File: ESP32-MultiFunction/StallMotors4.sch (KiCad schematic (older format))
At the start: 0 parts

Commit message: Working on ESP32-MultiFunction.
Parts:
- added C6, C7: .1 uf, Capacitors_SMD:C_0603, symbol C_Small
- added RR1: 10K Ohms, 48xxP:4814P, symbol 4814P-2
- added Term1: Motor 1, Connectors_Terminal_Blocks:TerminalBlock_Pheonix_MPT-2.54mm_5pol, symbol Screw_Terminal_01x05
- added Term2: Motor 2, Connectors_Terminal_Blocks:TerminalBlock_Pheonix_MPT-2.54mm_5pol, symbol Screw_Terminal_01x05
- added Term3: Motor 3, Connectors_Terminal_Blocks:TerminalBlock_Pheonix_MPT-2.54mm_5pol, symbol Screw_Terminal_01x05
- added Term4: Motor 4, Connectors_Terminal_Blocks:TerminalBlock_Pheonix_MPT-2.54mm_5pol, symbol Screw_Terminal_01x05
- added Term5: + 12V -, symbol Screw_Terminal_01x02
- added U2, U4: 74HCT00, Housings_SOIC:SOIC-14_3.9x8.7mm_Pitch1.27mm, symbol 74HCT00
- added U5, U6, U7, U8: TC4428, Housings_SOIC:SOIC-8_3.9x4.9mm_Pitch1.27mm, symbol TC4428
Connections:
- new net: U2.2, U2.6
- new net: U2.10, U2.11
- new net: U4.2, U4.6
- new net: U4.10, U4.11
- new net +12V: Term5.1 (Pin_1), U5.6 (Vdd), U5.6 (Vdd), U6.6 (Vdd), U6.6 (Vdd), U7.6 (Vdd), U7.6 (Vdd), U8.6 (Vdd), U8.6 (Vdd)
- new net +3V3: C6.1, C7.1, RR1.14 (Comm), U2.14 (VCC), U2.14 (VCC), U2.14 (VCC), U2.14 (VCC), U4.14 (VCC), U4.14 (VCC), U4.14 (VCC), U4.14 (VCC)
- new net GND: C6.2, C7.2, Term1.4 (Pin_4), Term2.4 (Pin_4), Term3.4 (Pin_4), Term4.4 (Pin_4), Term5.2 (Pin_2), U2.7 (GND), U2.7 (GND), U2.7 (GND), U2.7 (GND), U4.7 (GND), U4.7 (GND), U4.7 (GND), U4.7 (GND), U5.3 (GND), U5.3 (GND), U6.3 (GND), U6.3 (GND), U7.3 (GND), U7.3 (GND), U8.3 (GND), U8.3 (GND)
- new net M1A: Term1.1 (Pin_1), U5.7 (Out)
- new net M1B: Term1.2 (Pin_2), U5.5 (Out)
- new net M2A: Term2.1 (Pin_1), U6.7 (Out)
- new net M2B: Term2.2 (Pin_2), U6.5 (Out)
- new net M3A: Term3.1 (Pin_1), U7.7 (Out)
- new net M3B: Term3.2 (Pin_2), U7.5 (Out)
- new net M4A: Term4.1 (Pin_1), U8.7 (Out)
- new net M4B: Term4.2 (Pin_2), U8.5 (Out)
- new net Motor1: U5.2 (IN), U5.4 (IN)
- new net Motor2: U6.2 (IN), U6.4 (IN)
- new net Motor3: U7.2 (IN), U7.4 (IN)
- new net Motor4: U8.2 (IN), U8.4 (IN)
- new net P1A: RR1.6 (R6), Term1.3 (Pin_3), U2.1
- new net P1B: RR1.5 (R5), Term1.5 (Pin_5), U2.5
- new net P2A: RR1.4 (R4), Term2.3 (Pin_3), U2.9
- new net P2B: RR1.3 (R3), Term2.5 (Pin_5), U2.13
- new net P3A: RR1.13 (R13), Term3.3 (Pin_3), U4.1
- new net P3B: RR1.12 (R12), Term3.5 (Pin_5), U4.5
- new net P4A: RR1.11 (R11), Term4.3 (Pin_3), U4.9
- new net P4B: RR1.10 (R10), Term4.5 (Pin_5), U4.13
- new net Points1: U2.3, U2.4
- new net Points2: U2.12, U2.8
- new net Points3: U4.3, U4.4
- new net Points4: U4.12, U4.8
- no-connect marks 0 -> 5

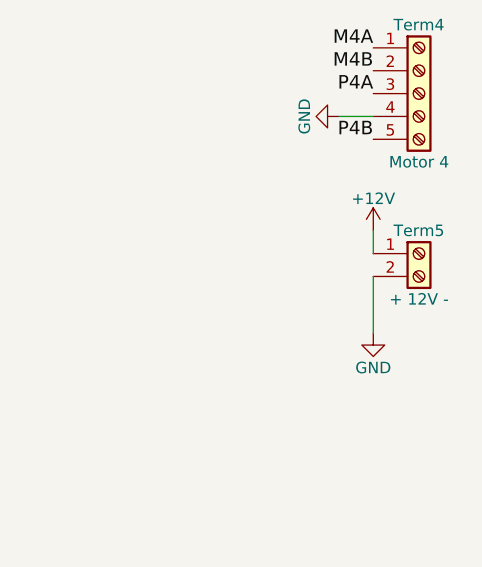
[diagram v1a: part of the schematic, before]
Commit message: Working on ESP32-MultiFunction.
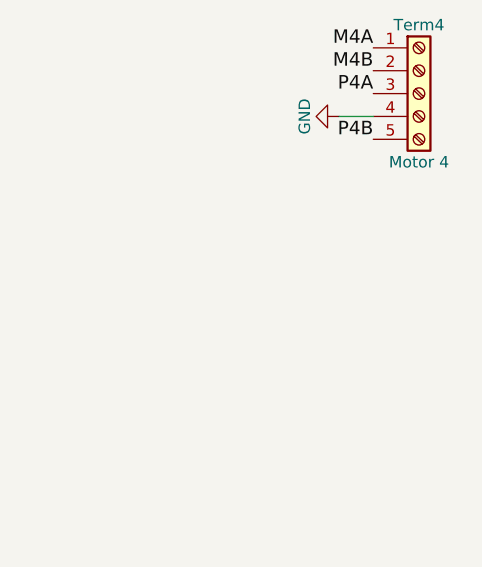
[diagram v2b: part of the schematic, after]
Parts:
- removed Term5: + 12V -, symbol Screw_Terminal_01x02
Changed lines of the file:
@@
 $Descr A4 11693 8268
 encoding utf-8
-Sheet 6 8
+Sheet 6 7
 Title "ESP32 Multifunction board"
 Date ""
@@
 	4500 2100 4500 2150
 $Comp
-L Screw_Terminal_01x02 Term5
-U 1 1 60CDEFA9
-P 10000 4300
-F 0 "Term5" H 10000 4400 50  0000 C CNN
-F 1 "+ 12V -" H 10000 4100 50  0000 C CNN
-F 2 "" H 10000 4300 50  0001 C CNN
-F 3 "" H 10000 4300 50  0001 C CNN
-	1    10000 4300
-	1    0    0    -1
-$EndComp
-$Comp
-L +12V #PWR45
-U 1 1 60CDEFFA
-P 9800 4200
-F 0 "#PWR45" H 9800 4050 50  0001 C CNN
-F 1 "+12V" H 9800 4340 50  0000 C CNN
-F 2 "" H 9800 4200 50  0001 C CNN
-F 3 "" H 9800 4200 50  0001 C CNN
-	1    9800 4200
-	1    0    0    -1
-$EndComp
-$Comp
-L GND #PWR46
-U 1 1 60CDF03E
-P 9800 4650
-F 0 "#PWR46" H 9800 4400 50  0001 C CNN
-F 1 "GND" H 9800 4500 50  0000 C CNN
-F 2 "" H 9800 4650 50  0001 C CNN
-F 3 "" H 9800 4650 50  0001 C CNN
-	1    9800 4650
-	1    0    0    -1
-$EndComp
-$Comp
 L GND #PWR42
 U 1 1 60CDF082
@@
 Wire Wire Line
 	9800 3700 9650 3700
-Wire Wire Line
-	9800 4200 9800 4300
-Wire Wire Line
-	9800 4400 9800 4650
 Text Label 9800 800  2    59   ~ 0
 M1A

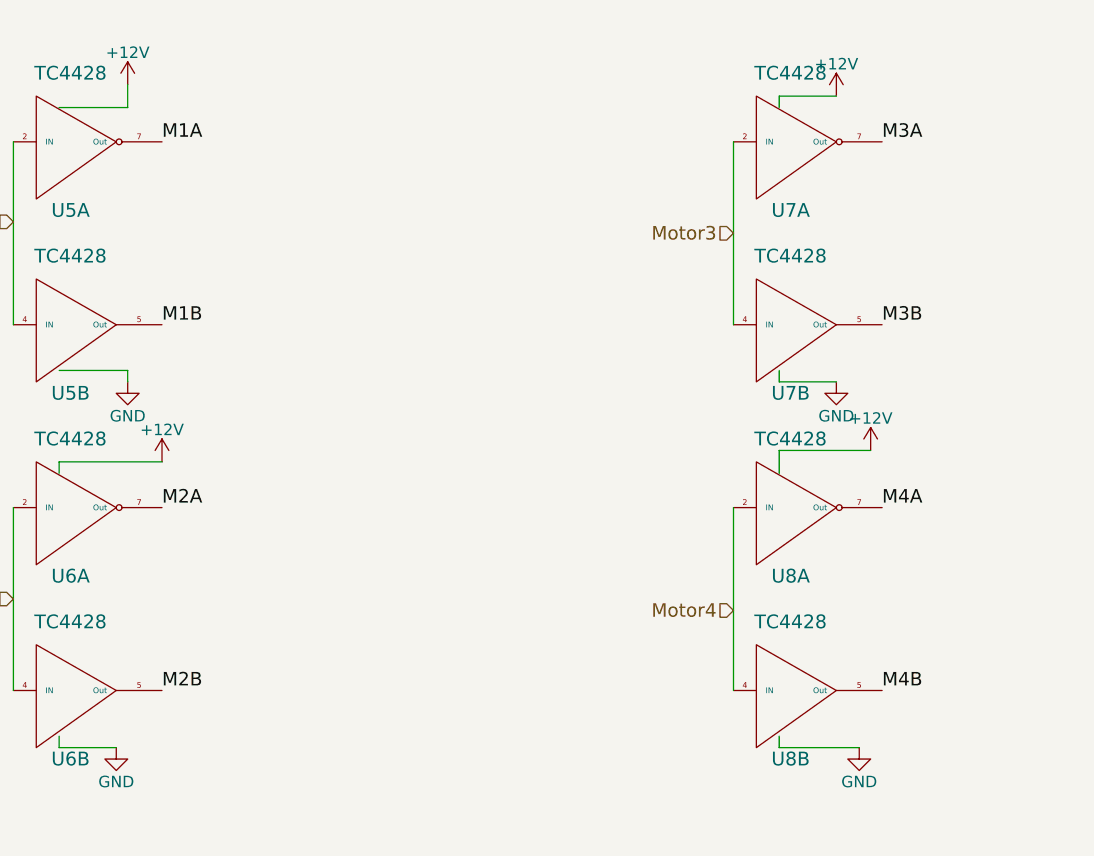
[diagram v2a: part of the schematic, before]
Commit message: Working on ESP32-MultiFunction.
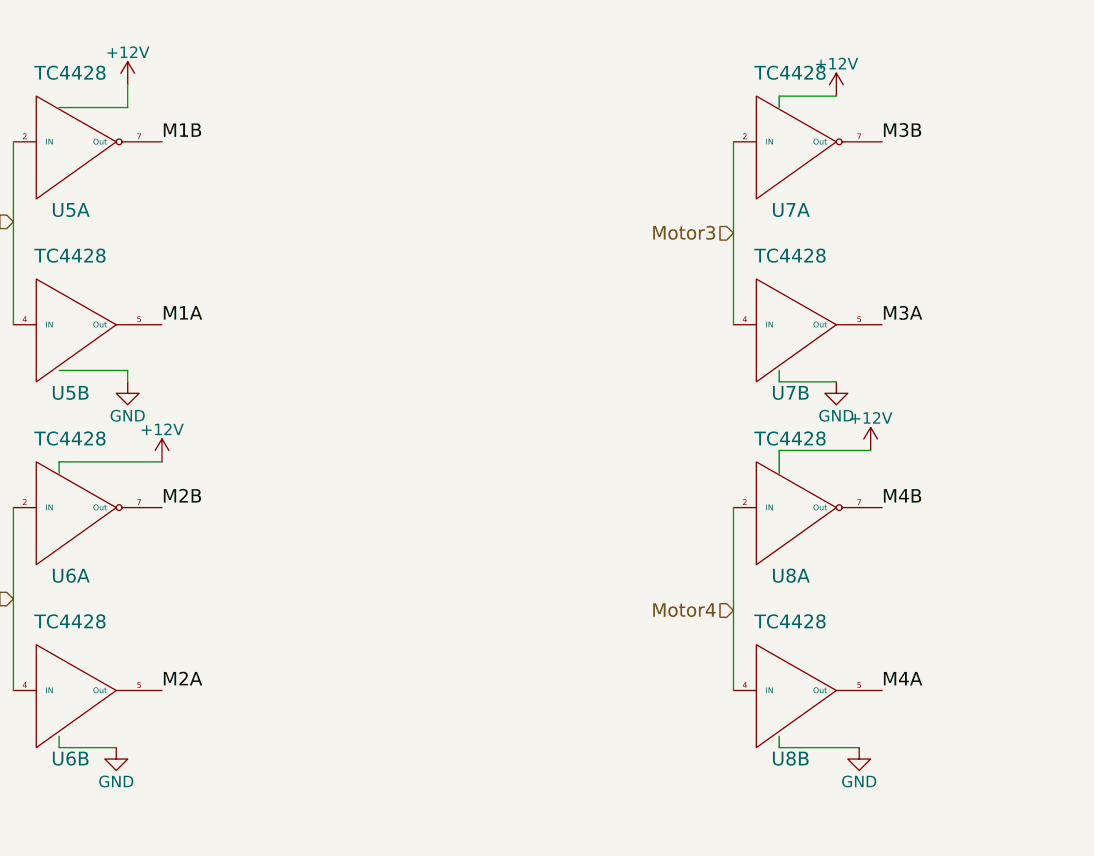
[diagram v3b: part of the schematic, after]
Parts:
- U2, U4: footprint (none) -> Housings_SOIC:SOIC-14_3.9x8.7mm_Pitch1.27mm
- U5, U6, U7, U8: footprint (none) -> Housings_SOIC:SOIC-8_3.9x4.9mm_Pitch1.27mm
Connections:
- net M1A: now also U5.5 (Out); no longer U5.7 (Out)
- net M1B: now also U5.7 (Out); no longer U5.5 (Out)
- net M2A: now also U6.5 (Out); no longer U6.7 (Out)
- net M2B: now also U6.7 (Out); no longer U6.5 (Out)
- net M3A: now also U7.5 (Out); no longer U7.7 (Out)
- net M3B: now also U7.7 (Out); no longer U7.5 (Out)
- net M4A: now also U8.5 (Out); no longer U8.7 (Out)
- net M4B: now also U8.7 (Out); no longer U8.5 (Out)
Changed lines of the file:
@@
 F 0 "U2" H 2000 1950 50  0000 C CNN
 F 1 "74HCT00" H 2000 1800 50  0000 C CNN
-F 2 "" H 2000 1900 50  0001 C CNN
+F 2 "Housings_SOIC:SOIC-14_3.9x8.7mm_Pitch1.27mm" H 2000 1900 50  0001 C CNN
 F 3 "" H 2000 1900 50  0001 C CNN
 	2    2000 1900
@@
 F 0 "U2" H 2000 2750 50  0000 C CNN
 F 1 "74HCT00" H 2000 2600 50  0000 C CNN
-F 2 "" H 2000 2700 50  0001 C CNN
+F 2 "Housings_SOIC:SOIC-14_3.9x8.7mm_Pitch1.27mm" H 2000 2700 50  0001 C CNN
 F 3 "" H 2000 2700 50  0001 C CNN
 	3    2000 2700
@@
 F 0 "U2" H 2000 3450 50  0000 C CNN
 F 1 "74HCT00" H 2000 3300 50  0000 C CNN
-F 2 "" H 2000 3400 50  0001 C CNN
+F 2 "Housings_SOIC:SOIC-14_3.9x8.7mm_Pitch1.27mm" H 2000 3400 50  0001 C CNN
 F 3 "" H 2000 3400 50  0001 C CNN
 	4    2000 3400
@@
 F 0 "U4" H 2050 5350 50  0000 C CNN
 F 1 "74HCT00" H 2050 5200 50  0000 C CNN
-F 2 "" H 2050 5300 50  0001 C CNN
+F 2 "Housings_SOIC:SOIC-14_3.9x8.7mm_Pitch1.27mm" H 2050 5300 50  0001 C CNN
 F 3 "" H 2050 5300 50  0001 C CNN
 	2    2050 5300
@@
 F 0 "U4" H 2050 6150 50  0000 C CNN
 F 1 "74HCT00" H 2050 6000 50  0000 C CNN
-F 2 "" H 2050 6100 50  0001 C CNN
+F 2 "Housings_SOIC:SOIC-14_3.9x8.7mm_Pitch1.27mm" H 2050 6100 50  0001 C CNN
 F 3 "" H 2050 6100 50  0001 C CNN
 	3    2050 6100
@@
 F 0 "U4" H 2050 6850 50  0000 C CNN
 F 1 "74HCT00" H 2050 6700 50  0000 C CNN
-F 2 "" H 2050 6800 50  0001 C CNN
+F 2 "Housings_SOIC:SOIC-14_3.9x8.7mm_Pitch1.27mm" H 2050 6800 50  0001 C CNN
 F 3 "" H 2050 6800 50  0001 C CNN
 	4    2050 6800
@@
 F 0 "U5" H 4250 1600 60  0000 C CNN
 F 1 "TC4428" H 4250 2200 60  0000 C CNN
-F 2 "" H 4250 1900 60  0000 C CNN
+F 2 "Housings_SOIC:SOIC-8_3.9x4.9mm_Pitch1.27mm" H 4250 1900 60  0001 C CNN
 F 3 "" H 4250 1900 60  0000 C CNN
 	2    4250 1900
@@
 F 0 "U6" H 4250 3200 60  0000 C CNN
 F 1 "TC4428" H 4250 3800 60  0000 C CNN
-F 2 "" H 4250 3500 60  0000 C CNN
+F 2 "Housings_SOIC:SOIC-8_3.9x4.9mm_Pitch1.27mm" H 4250 3500 60  0001 C CNN
 F 3 "" H 4250 3500 60  0000 C CNN
 	2    4250 3500
@@
 F 0 "U7" H 7400 1600 60  0000 C CNN
 F 1 "TC4428" H 7400 2200 60  0000 C CNN
-F 2 "" H 7400 1900 60  0000 C CNN
+F 2 "Housings_SOIC:SOIC-8_3.9x4.9mm_Pitch1.27mm" H 7400 1900 60  0001 C CNN
 F 3 "" H 7400 1900 60  0000 C CNN
 	2    7400 1900
@@
 F 0 "U8" H 7400 3200 60  0000 C CNN
 F 1 "TC4428" H 7400 3800 60  0000 C CNN
-F 2 "" H 7400 3500 60  0000 C CNN
+F 2 "Housings_SOIC:SOIC-8_3.9x4.9mm_Pitch1.27mm" H 7400 3500 60  0001 C CNN
 F 3 "" H 7400 3500 60  0000 C CNN
 	2    7400 3500
@@
 $Comp
 L Screw_Terminal_01x05 Term1
-U 1 1 60CD6A0E
+U 1 1 60CF9376
 P 10000 1000
 F 0 "Term1" H 10000 1300 50  0000 C CNN
@@
 $EndComp
 $Comp
-L +3V3 #PWR28
+L +3V3 #PWR036
 U 1 1 60CD8400
 P 1800 750
-F 0 "#PWR28" H 1800 600 50  0001 C CNN
+F 0 "#PWR036" H 1800 600 50  0001 C CNN
 F 1 "+3V3" H 1800 890 50  0000 C CNN
 F 2 "" H 1800 750 50  0001 C CNN
@@
 $EndComp
 $Comp
-L +3V3 #PWR30
+L +3V3 #PWR037
 U 1 1 60CD84B5
 P 1800 4200
-F 0 "#PWR30" H 1800 4050 50  0001 C CNN
+F 0 "#PWR037" H 1800 4050 50  0001 C CNN
 F 1 "+3V3" H 1800 4340 50  0000 C CNN
 F 2 "" H 1800 4200 50  0001 C CNN
@@
 $EndComp
 $Comp
-L GND #PWR29
+L GND #PWR038
 U 1 1 60CD85AF
 P 1800 3800
-F 0 "#PWR29" H 1800 3550 50  0001 C CNN
+F 0 "#PWR038" H 1800 3550 50  0001 C CNN
 F 1 "GND" H 1800 3650 50  0000 C CNN
 F 2 "" H 1800 3800 50  0001 C CNN
@@
 $EndComp
 $Comp
-L GND #PWR31
+L GND #PWR039
 U 1 1 60CD86EE
 P 1850 7200
-F 0 "#PWR31" H 1850 6950 50  0001 C CNN
+F 0 "#PWR039" H 1850 6950 50  0001 C CNN
 F 1 "GND" H 1850 7050 50  0000 C CNN
 F 2 "" H 1850 7200 50  0001 C CNN
@@
 	3200 1050 2850 1050
 $Comp
-L GND #PWR32
+L GND #PWR040
 U 1 1 60CD9FDD
 P 3200 1200
-F 0 "#PWR32" H 3200 950 50  0001 C CNN
+F 0 "#PWR040" H 3200 950 50  0001 C CNN
 F 1 "GND" H 3200 1050 50  0000 C CNN
 F 2 "" H 3200 1200 50  0001 C CNN
@@
 P4B
 Text Label 4650 1100 0    59   ~ 0
+M1B
+Text Label 4650 1900 0    59   ~ 0
 M1A
-Text Label 4650 1900 0    59   ~ 0
-M1B
 Text Label 4650 2700 0    59   ~ 0
+M2B
+Text Label 4650 3500 0    59   ~ 0
 M2A
-Text Label 4650 3500 0    59   ~ 0
-M2B
 Text Label 7800 1100 0    59   ~ 0
+M3B
+Text Label 7800 1900 0    59   ~ 0
 M3A
-Text Label 7800 1900 0    59   ~ 0
-M3B
 Text Label 7800 2700 0    59   ~ 0
+M4B
+Text Label 7800 3500 0    59   ~ 0
 M4A
-Text Label 7800 3500 0    59   ~ 0
-M4B
 Wire Wire Line
 	7150 2700 7150 3500
@@
 Motor4
 $Comp
-L GND #PWR35
+L GND #PWR041
 U 1 1 60CDE058
 P 4500 2150
-F 0 "#PWR35" H 4500 1900 50  0001 C CNN
+F 0 "#PWR041" H 4500 1900 50  0001 C CNN
 F 1 "GND" H 4500 2000 50  0000 C CNN
 F 2 "" H 4500 2150 50  0001 C CNN
@@
 $EndComp
 $Comp
-L GND #PWR38
+L GND #PWR042
 U 1 1 60CDE09A
 P 7600 2150
-F 0 "#PWR38" H 7600 1900 50  0001 C CNN
+F 0 "#PWR042" H 7600 1900 50  0001 C CNN
 F 1 "GND" H 7600 2000 50  0000 C CNN
 F 2 "" H 7600 2150 50  0001 C CNN
@@
 $EndComp
 $Comp
-L GND #PWR33
+L GND #PWR043
 U 1 1 60CDE17D
 P 4450 3750
-F 0 "#PWR33" H 4450 3500 50  0001 C CNN
+F 0 "#PWR043" H 4450 3500 50  0001 C CNN
 F 1 "GND" H 4450 3600 50  0000 C CNN
 F 2 "" H 4450 3750 50  0001 C CNN
@@
 $EndComp
 $Comp
-L GND #PWR39
+L GND #PWR044
 U 1 1 60CDE1BF
 P 7700 3750
-F 0 "#PWR39" H 7700 3500 50  0001 C CNN
+F 0 "#PWR044" H 7700 3500 50  0001 C CNN
 F 1 "GND" H 7700 3600 50  0000 C CNN
 F 2 "" H 7700 3750 50  0001 C CNN
@@
 $EndComp
 $Comp
-L +12V #PWR34
+L +12V #PWR045
 U 1 1 60CDE3F5
 P 4500 850
-F 0 "#PWR34" H 4500 700 50  0001 C CNN
+F 0 "#PWR045" H 4500 700 50  0001 C CNN
 F 1 "+12V" H 4500 990 50  0000 C CNN
 F 2 "" H 4500 850 50  0001 C CNN
@@
 $EndComp
 $Comp
-L +12V #PWR37
+L +12V #PWR046
 U 1 1 60CDE437
 P 7600 900
-F 0 "#PWR37" H 7600 750 50  0001 C CNN
+F 0 "#PWR046" H 7600 750 50  0001 C CNN
 F 1 "+12V" H 7600 1040 50  0000 C CNN
 F 2 "" H 7600 900 50  0001 C CNN
@@
 $EndComp
 $Comp
-L +12V #PWR40
+L +12V #PWR047
 U 1 1 60CDE58D
 P 7750 2450
-F 0 "#PWR40" H 7750 2300 50  0001 C CNN
+F 0 "#PWR047" H 7750 2300 50  0001 C CNN
 F 1 "+12V" H 7750 2590 50  0000 C CNN
 F 2 "" H 7750 2450 50  0001 C CNN
@@
 $EndComp
 $Comp
-L +12V #PWR36
+L +12V #PWR048
 U 1 1 60CDE691
 P 4650 2500
-F 0 "#PWR36" H 4650 2350 50  0001 C CNN
+F 0 "#PWR048" H 4650 2350 50  0001 C CNN
 F 1 "+12V" H 4650 2640 50  0000 C CNN
 F 2 "" H 4650 2500 50  0001 C CNN
@@
 	4500 2100 4500 2150
 $Comp
-L GND #PWR42
+L GND #PWR049
 U 1 1 60CDF082
 P 9650 3700
-F 0 "#PWR42" H 9650 3450 50  0001 C CNN
+F 0 "#PWR049" H 9650 3450 50  0001 C CNN
 F 1 "GND" H 9650 3550 50  0000 C CNN
 F 2 "" H 9650 3700 50  0001 C CNN
@@
 $EndComp
 $Comp
-L GND #PWR41
+L GND #PWR050
 U 1 1 60CDF132
 P 9650 2750
-F 0 "#PWR41" H 9650 2500 50  0001 C CNN
+F 0 "#PWR050" H 9650 2500 50  0001 C CNN
 F 1 "GND" H 9650 2600 50  0000 C CNN
 F 2 "" H 9650 2750 50  0001 C CNN
@@
 $EndComp
 $Comp
-L GND #PWR44
+L GND #PWR051
 U 1 1 60CDF3BC
 P 9700 1900
-F 0 "#PWR44" H 9700 1650 50  0001 C CNN
+F 0 "#PWR051" H 9700 1650 50  0001 C CNN
 F 1 "GND" H 9700 1750 50  0000 C CNN
 F 2 "" H 9700 1900 50  0001 C CNN
@@
 $EndComp
 $Comp
-L GND #PWR43
+L GND #PWR052
 U 1 1 60CDF400
 P 9700 1100
-F 0 "#PWR43" H 9700 850 50  0001 C CNN
+F 0 "#PWR052" H 9700 850 50  0001 C CNN
 F 1 "GND" H 9700 950 50  0000 C CNN
 F 2 "" H 9700 1100 50  0001 C CNN

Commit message: Fixes to MegaIOOpenMRN 64 Line Hardware.hxx.
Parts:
- C6, C7: symbol C_Small -> ESP32-MultiFunction-rescue:C_Small
- RR1: symbol 4814P-2 -> ESP32-MultiFunction-rescue:4814P-2
- Term1, Term2, Term3, Term4: symbol Screw_Terminal_01x05 -> ESP32-MultiFunction-rescue:Screw_Terminal_01x05
- U2, U4: symbol 74HCT00 -> ESP32-MultiFunction-rescue:74HCT00
- U5, U6, U7, U8: symbol TC4428 -> ESP32-MultiFunction-rescue:TC4428
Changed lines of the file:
@@
-EESchema Schematic File Version 2
-LIBS:power
-LIBS:device
-LIBS:switches
-LIBS:relays
-LIBS:motors
-LIBS:transistors
-LIBS:conn
-LIBS:linear
-LIBS:regul
-LIBS:74xx
-LIBS:cmos4000
-LIBS:adc-dac
-LIBS:memory
-LIBS:xilinx
-LIBS:microcontrollers
-LIBS:dsp
-LIBS:microchip
-LIBS:analog_switches
-LIBS:motorola
-LIBS:texas
-LIBS:intel
-LIBS:audio
-LIBS:interface
-LIBS:digital-audio
-LIBS:philips
-LIBS:display
-LIBS:cypress
-LIBS:siliconi
-LIBS:opto
-LIBS:atmel
-LIBS:contrib
-LIBS:esp32_devboards
-LIBS:sn65hvd233-ht
-LIBS:lm2574n-5
-LIBS:MCP23xxx
-LIBS:tbd62x83a
-LIBS:tc442x
-LIBS:mct6h
-LIBS:bridge
-LIBS:pca9685
-LIBS:4814p-2
-LIBS:mechanical
-LIBS:graphic_symbols
-LIBS:references
+EESchema Schematic File Version 4
 LIBS:ESP32-MultiFunction-cache
-EELAYER 25 0
+EELAYER 30 0
 EELAYER END
 $Descr A4 11693 8268
@@
 $EndDescr
 $Comp
-L 74HCT00 U2
+L ESP32-MultiFunction-rescue:74HCT00 U2
 U 2 1 60CD31DC
 P 2000 1900
@@
 $EndComp
 $Comp
-L 74HCT00 U2
+L ESP32-MultiFunction-rescue:74HCT00 U2
 U 3 1 60CD3211
 P 2000 2700
@@
 $EndComp
 $Comp
-L 74HCT00 U2
+L ESP32-MultiFunction-rescue:74HCT00 U2
 U 4 1 60CD324F
 P 2000 3400
@@
 $EndComp
 $Comp
-L 74HCT00 U4
+L ESP32-MultiFunction-rescue:74HCT00 U4
 U 1 1 60CD3BDA
 P 2050 4600
@@
 $EndComp
 $Comp
-L 74HCT00 U4
+L ESP32-MultiFunction-rescue:74HCT00 U4
 U 2 1 60CD3BE0
 P 2050 5300
@@
 $EndComp
 $Comp
-L 74HCT00 U4
+L ESP32-MultiFunction-rescue:74HCT00 U4
 U 3 1 60CD3BE6
 P 2050 6100
@@
 $EndComp
 $Comp
-L 74HCT00 U4
+L ESP32-MultiFunction-rescue:74HCT00 U4
 U 4 1 60CD3BEC
 P 2050 6800
@@
 $EndComp
 $Comp
-L 4814P-2 RR1
+L ESP32-MultiFunction-rescue:4814P-2 RR1
 U 1 1 60CD4592
 P 900 4200
@@
 $EndComp
 $Comp
-L C_Small C6
+L ESP32-MultiFunction-rescue:C_Small C6
 U 1 1 60CD54EA
 P 2850 950
@@
 $EndComp
 $Comp
-L C_Small C7
+L ESP32-MultiFunction-rescue:C_Small C7
 U 1 1 60CD553D
 P 3200 950
@@
 $EndComp
 $Comp
-L TC4428 U5
+L ESP32-MultiFunction-rescue:TC4428 U5
 U 1 1 60CD5772
 P 4250 1100
@@
 $EndComp
 $Comp
-L TC4428 U5
+L ESP32-MultiFunction-rescue:TC4428 U5
 U 2 1 60CD57A9
 P 4250 1900
@@
 $EndComp
 $Comp
-L TC4428 U6
+L ESP32-MultiFunction-rescue:TC4428 U6
 U 1 1 60CD593C
 P 4250 2700
@@
 $EndComp
 $Comp
-L TC4428 U6
+L ESP32-MultiFunction-rescue:TC4428 U6
 U 2 1 60CD5AD3
 P 4250 3500
@@
 $EndComp
 $Comp
-L TC4428 U7
+L ESP32-MultiFunction-rescue:TC4428 U7
 U 1 1 60CD5B99
 P 7400 1100
@@
 $EndComp
 $Comp
-L TC4428 U7
+L ESP32-MultiFunction-rescue:TC4428 U7
 U 2 1 60CD5DFA
 P 7400 1900
@@
 $EndComp
 $Comp
-L TC4428 U8
+L ESP32-MultiFunction-rescue:TC4428 U8
 U 1 1 60CD5F16
 P 7400 2700
@@
 $EndComp
 $Comp
-L TC4428 U8
+L ESP32-MultiFunction-rescue:TC4428 U8
 U 2 1 60CD5F79
 P 7400 3500
@@
 $EndComp
 $Comp
-L Screw_Terminal_01x05 Term1
+L ESP32-MultiFunction-rescue:Screw_Terminal_01x05 Term1
 U 1 1 60CF9376
 P 10000 1000
@@
 $EndComp
 $Comp
-L Screw_Terminal_01x05 Term2
+L ESP32-MultiFunction-rescue:Screw_Terminal_01x05 Term2
 U 1 1 60CD6A61
 P 10000 1800
@@
 $EndComp
 $Comp
-L Screw_Terminal_01x05 Term3
+L ESP32-MultiFunction-rescue:Screw_Terminal_01x05 Term3
 U 1 1 60CD6B08
 P 10000 2650
@@
 $EndComp
 $Comp
-L Screw_Terminal_01x05 Term4
+L ESP32-MultiFunction-rescue:Screw_Terminal_01x05 Term4
 U 1 1 60CD6C75
 P 10000 3600
@@
 $EndComp
 $Comp
-L +3V3 #PWR036
+L ESP32-MultiFunction-rescue:+3V3 #PWR036
 U 1 1 60CD8400
 P 1800 750
@@
 $EndComp
 $Comp
-L +3V3 #PWR037
+L ESP32-MultiFunction-rescue:+3V3 #PWR037
 U 1 1 60CD84B5
 P 1800 4200
@@
 $EndComp
 $Comp
-L GND #PWR038
+L ESP32-MultiFunction-rescue:GND #PWR038
 U 1 1 60CD85AF
 P 1800 3800
@@
 $EndComp
 $Comp
-L GND #PWR039
+L ESP32-MultiFunction-rescue:GND #PWR039
 U 1 1 60CD86EE
 P 1850 7200
@@
 	1800 750  1800 1000
 $Comp
-L 74HCT00 U2
+L ESP32-MultiFunction-rescue:74HCT00 U2
 U 1 1 60CD316F
 P 2000 1200
@@
 	3200 1050 2850 1050
 $Comp
-L GND #PWR040
+L ESP32-MultiFunction-rescue:GND #PWR040
 U 1 1 60CD9FDD
 P 3200 1200
@@
 Motor4
 $Comp
-L GND #PWR041
+L ESP32-MultiFunction-rescue:GND #PWR041
 U 1 1 60CDE058
 P 4500 2150
@@
 $EndComp
 $Comp
-L GND #PWR042
+L ESP32-MultiFunction-rescue:GND #PWR042
 U 1 1 60CDE09A
 P 7600 2150
@@
 $EndComp
 $Comp
-L GND #PWR043
+L ESP32-MultiFunction-rescue:GND #PWR043
 U 1 1 60CDE17D
 P 4450 3750
@@
 $EndComp
 $Comp
-L GND #PWR044
+L ESP32-MultiFunction-rescue:GND #PWR044
 U 1 1 60CDE1BF
 P 7700 3750
@@
 $EndComp
 $Comp
-L +12V #PWR045
+L ESP32-MultiFunction-rescue:+12V #PWR045
 U 1 1 60CDE3F5
 P 4500 850
+AR Path="/60CDE3F5" Ref="#PWR045"  Part="1"
+AR Path="/60CD422F/60CDE3F5" Ref="#PWR045"  Part="1"
 F 0 "#PWR045" H 4500 700 50  0001 C CNN
 F 1 "+12V" H 4500 990 50  0000 C CNN
@@
 $EndComp
 $Comp
-L +12V #PWR046
+L ESP32-MultiFunction-rescue:+12V #PWR046
 U 1 1 60CDE437
 P 7600 900
+AR Path="/60CDE437" Ref="#PWR046"  Part="1"
+AR Path="/60CD422F/60CDE437" Ref="#PWR046"  Part="1"
 F 0 "#PWR046" H 7600 750 50  0001 C CNN
 F 1 "+12V" H 7600 1040 50  0000 C CNN
@@
 $EndComp
 $Comp
-L +12V #PWR047
+L ESP32-MultiFunction-rescue:+12V #PWR047
 U 1 1 60CDE58D
 P 7750 2450
+AR Path="/60CDE58D" Ref="#PWR047"  Part="1"
+AR Path="/60CD422F/60CDE58D" Ref="#PWR047"  Part="1"
 F 0 "#PWR047" H 7750 2300 50  0001 C CNN
 F 1 "+12V" H 7750 2590 50  0000 C CNN
@@
 $EndComp
 $Comp
-L +12V #PWR048
+L ESP32-MultiFunction-rescue:+12V #PWR048
 U 1 1 60CDE691
 P 4650 2500
+AR Path="/60CDE691" Ref="#PWR048"  Part="1"
+AR Path="/60CD422F/60CDE691" Ref="#PWR048"  Part="1"
 F 0 "#PWR048" H 4650 2350 50  0001 C CNN
 F 1 "+12V" H 4650 2640 50  0000 C CNN
@@
 	4500 2100 4500 2150
 $Comp
-L GND #PWR049
+L ESP32-MultiFunction-rescue:GND #PWR049
 U 1 1 60CDF082
 P 9650 3700
@@
 $EndComp
 $Comp
-L GND #PWR050
+L ESP32-MultiFunction-rescue:GND #PWR050
 U 1 1 60CDF132
 P 9650 2750
@@
 $EndComp
 $Comp
-L GND #PWR051
+L ESP32-MultiFunction-rescue:GND #PWR051
 U 1 1 60CDF3BC
 P 9700 1900
@@
 $EndComp
 $Comp
-L GND #PWR052
+L ESP32-MultiFunction-rescue:GND #PWR052
 U 1 1 60CDF400
 P 9700 1100
